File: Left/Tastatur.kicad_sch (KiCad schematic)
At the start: 66 parts, among them J101 Conn_02x05_Counter_Clockwise, J102 Conn_01x04_Pin, J103 XT60PW-M, Q101 SI2301CDS-T1-GE3, Q102 SI2301CDS-T1-GE3, Q103 SI2301CDS-T1-GE3, Q104 SI2301CDS-T1-GE3, Q105 SI2301CDS-T1-GE3, Q106 2N7002HW, Q107 SI2301CDS-T1-GE3, SW221 MK-12C02-G020, U101 USBLC6-2SC6, U102 CH592F, U103 AP2112K-3.3, U104 MT3608, U105 TP4056-42-ESOP8, U106 CD4052B, U107 LM393, Y101 32MHz

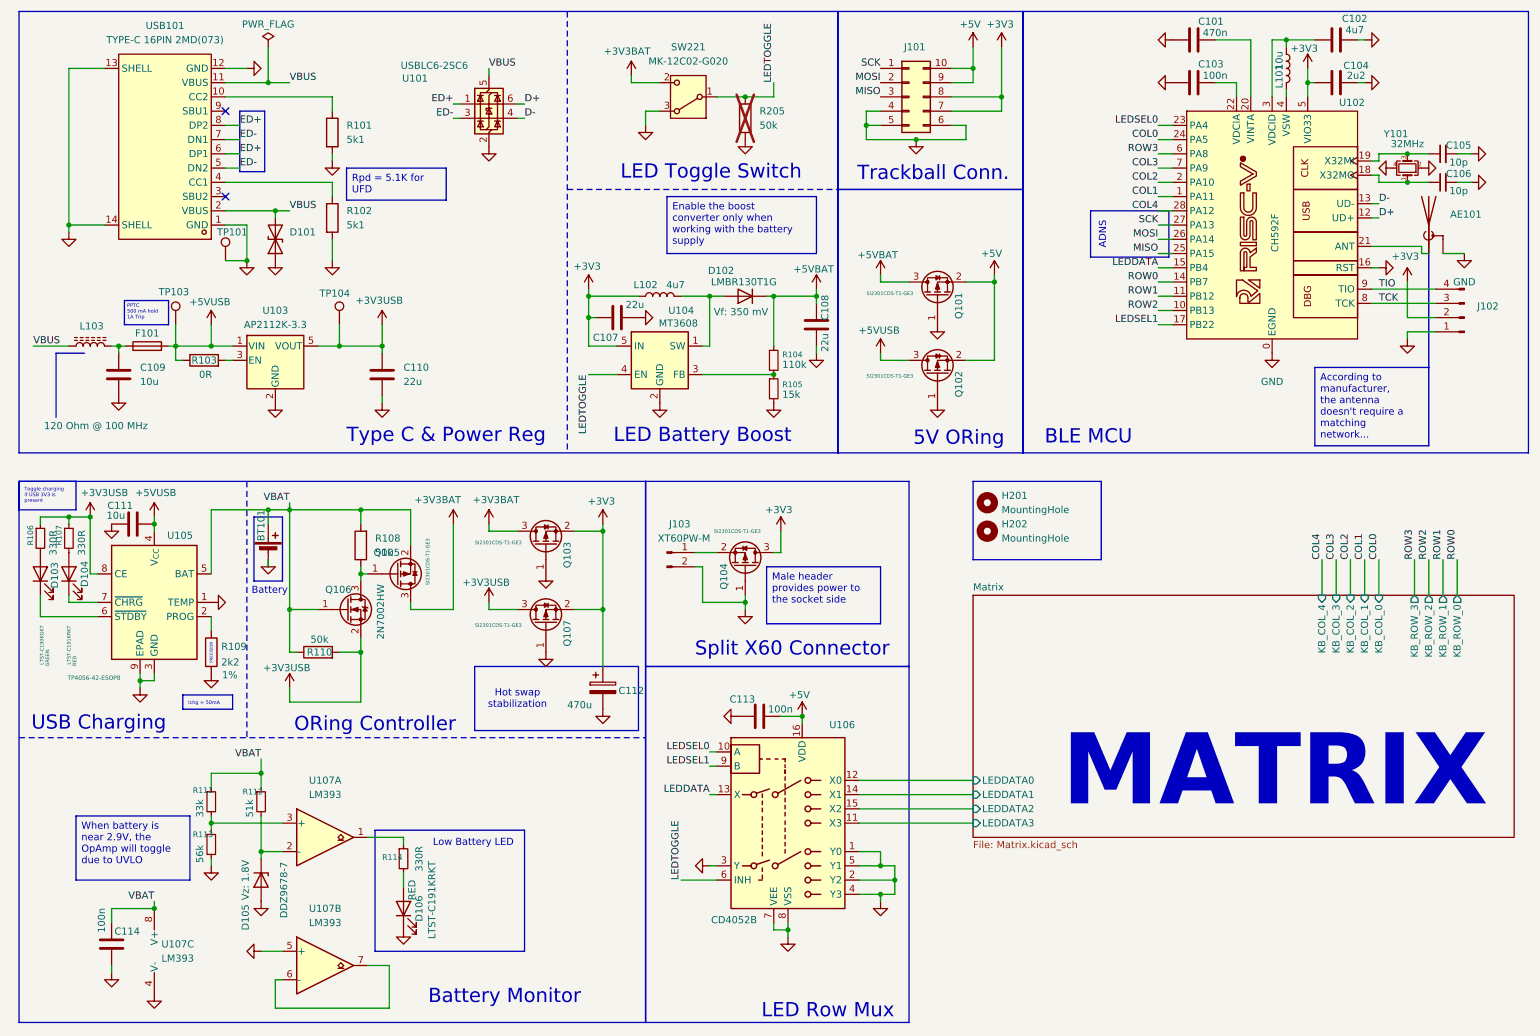
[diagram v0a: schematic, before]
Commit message: update design to use CH582F
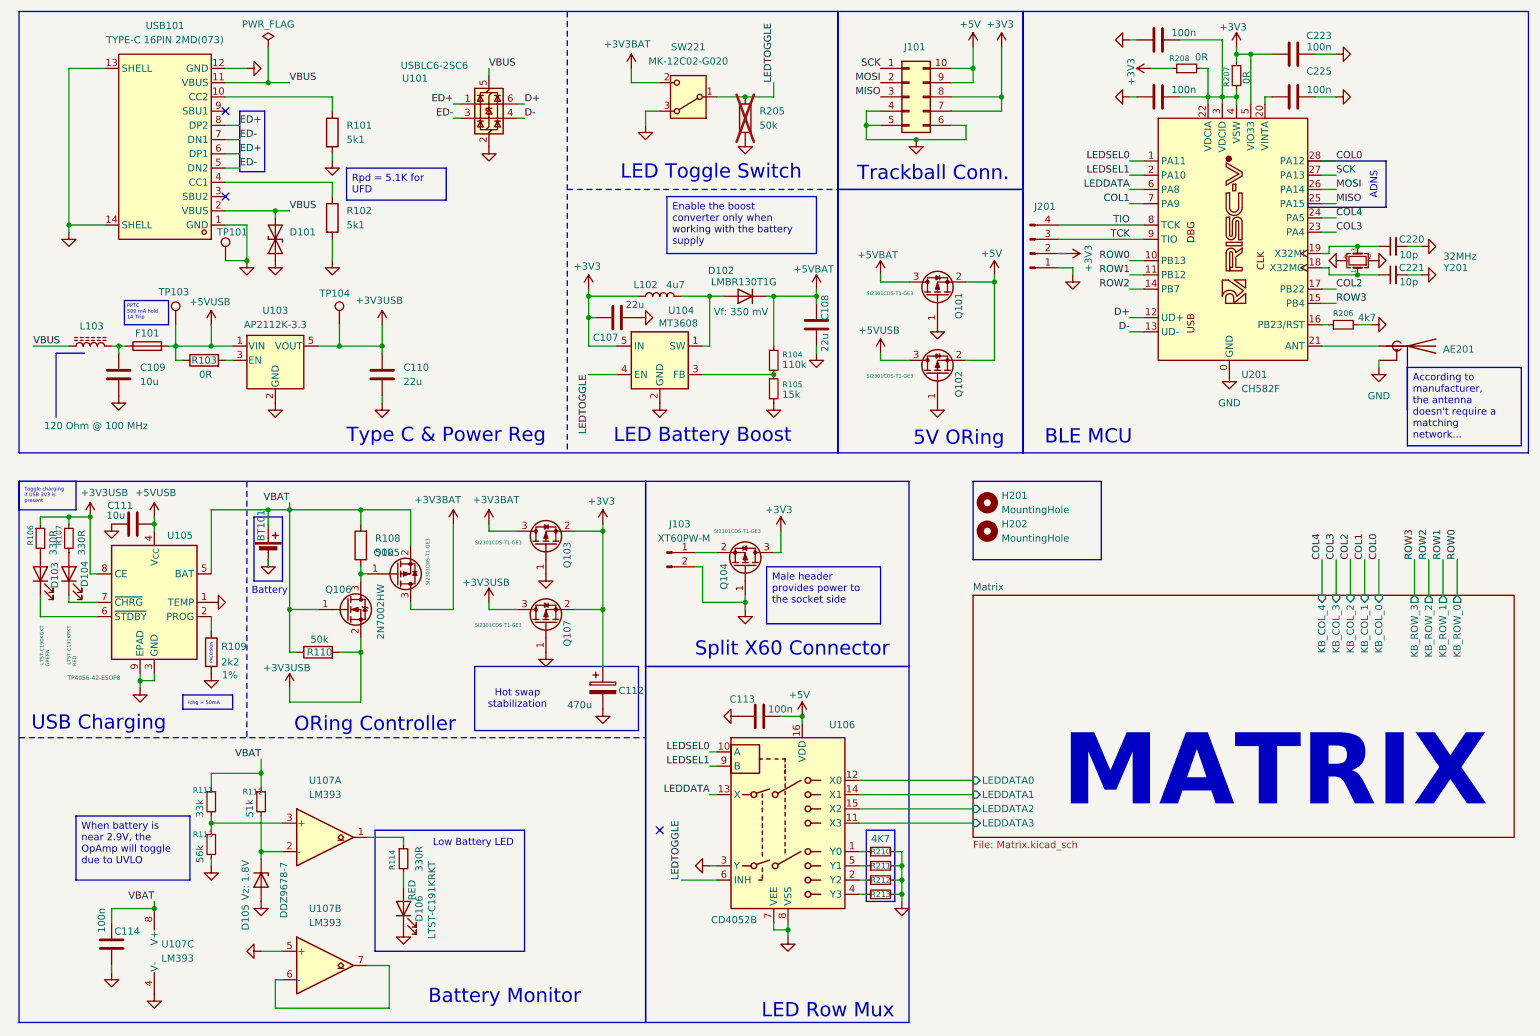
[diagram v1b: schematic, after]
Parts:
- removed AE101: Antenna_Shield, Inductor_SMD:L_1206_3216Metric, symbol Device:Antenna_Shield
- removed C101: 470n, Capacitor_SMD:C_0603_1608Metric_Pad1.08x0.95mm_HandSolder, symbol Device:C
- removed C102: 4u7, Capacitor_SMD:C_0603_1608Metric_Pad1.08x0.95mm_HandSolder, symbol Device:C
- removed C103: 100n, Capacitor_SMD:C_0603_1608Metric_Pad1.08x0.95mm_HandSolder, symbol Device:C
- removed C104: 2u2, Capacitor_SMD:C_0603_1608Metric_Pad1.08x0.95mm_HandSolder, symbol Device:C
- removed C105, C106: 10p, Capacitor_SMD:C_0603_1608Metric_Pad1.08x0.95mm_HandSolder, symbol Device:C_Small
- removed J102: Conn_01x04_Pin, Connector_JST:JST_PH_B4B-PH-K_1x04_P2.00mm_Vertical, symbol Connector:Conn_01x04_Pin
- removed L101: 10u, Inductor_SMD:L_0603_1608Metric_Pad1.05x0.95mm_HandSolder, symbol Device:L
- removed U102: CH592F, steew:CH592F, symbol steew:CH592F
- removed Y101: 32MHz, Crystal:Crystal_SMD_2016-4Pin_2.0x1.6mm, symbol Device:Crystal_GND24_Small
- added AE201: Antenna_Shield, Inductor_SMD:L_1206_3216Metric, symbol Device:Antenna_Shield
- added C220, C221: 10p, Capacitor_SMD:C_0603_1608Metric_Pad1.08x0.95mm_HandSolder, symbol Device:C_Small
- added C222, C223, C225, C226: 100n, Capacitor_SMD:C_0603_1608Metric_Pad1.08x0.95mm_HandSolder, symbol Device:C
- added J201: Conn_01x04_Pin, Connector_JST:JST_PH_B4B-PH-K_1x04_P2.00mm_Vertical, symbol Connector:Conn_01x04_Pin
- added R206: 4k7, Resistor_SMD:R_0603_1608Metric_Pad0.98x0.95mm_HandSolder, symbol Device:R_Small
- added R207, R208: 0R, Resistor_SMD:R_0603_1608Metric_Pad0.98x0.95mm_HandSolder, symbol Device:R_Small
- added R210, R211, R212, R213: 4K7, Resistor_SMD:R_0603_1608Metric_Pad0.98x0.95mm_HandSolder, symbol Device:R_Small
- added U201: CH582F, steew:CH582F, symbol steew:CH582F
- added Y201: 32MHz, Crystal:Crystal_SMD_2016-4Pin_2.0x1.6mm, symbol Device:Crystal_GND24_Small
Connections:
- net +3V3: now also C223.2, J201.2 (Pin_2), R207.1, R208.1, U201.5 (VIO33)
- net COL0: now also U201.28 (PA12)
- net COL1: now also U201.7 (PA9)
- net COL2: now also U201.17 (PB22)
- net COL3: now also U201.23 (PA4)
- net COL4: now also U201.24 (PA5)
- net D+: now also U201.12 (UD+)
- net D-: now also U201.13 (UD-)
- net GND: now also AE201.2 (Shield), C220.2, C221.2, C222.2, C223.1, C225.1, C226.2, J201.1 (Pin_1), R206.2, R210.2, R211.2, R212.2, R213.2, U201.0 (GND), Y201.2, Y201.4; no longer U106.1 (Y0), U106.2 (Y2), U106.4 (Y3), U106.5 (Y1)
- net LEDDATA: now also U201.6 (PA8)
- net LEDSEL0: now also U201.1 (PA11)
- net LEDSEL1: now also U201.2 (PA10)
- net MISO: now also U201.25 (PA15)
- net MOSI: now also U201.26 (PA14)
- net ROW0: now also U201.10 (PB13)
- net ROW1: now also U201.11 (PB12)
- net ROW2: now also U201.14 (PB7)
- net ROW3: now also U201.15 (PB4)
- net SCK: now also U201.27 (PA13)
- net TCK: now also J201.3 (Pin_3), U201.9 (TIO)
- net TIO: now also J201.4 (Pin_4), U201.8 (TCK)
- new net: R211.1, U106.5 (Y1)
- new net: R206.1, U201.16 (PB23/RST)
- new net: C222.1, C226.1, R207.2, R208.2, U201.22 (VDCIA), U201.3 (VDCID), U201.4 (VSW)
- new net: C221.1, U201.18 (X32MO), Y201.1
- new net: C220.1, U201.19 (X32MI), Y201.3
- new net: C225.2, U201.20 (VINTA)
- new net: AE201.1 (A), U201.21 (ANT)
- new net: R210.1, U106.1 (Y0)
- new net: R212.1, U106.2 (Y2)
- new net: R213.1, U106.4 (Y3)
- no-connect marks 2 -> 3

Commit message: redesign with smaller components
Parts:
- removed AE201: Antenna_Shield, Inductor_SMD:L_1206_3216Metric, symbol Device:Antenna_Shield
- removed C220, C221: 10p, Capacitor_SMD:C_0603_1608Metric_Pad1.08x0.95mm_HandSolder, symbol Device:C_Small
- removed C222, C223, C225, C226: 100n, Capacitor_SMD:C_0603_1608Metric_Pad1.08x0.95mm_HandSolder, symbol Device:C
- removed J101: Conn_02x05_Counter_Clockwise, symbol Connector_Generic:Conn_02x05_Counter_Clockwise
- removed J201: Conn_01x04_Pin, Connector_JST:JST_PH_B4B-PH-K_1x04_P2.00mm_Vertical, symbol Connector:Conn_01x04_Pin
- removed Q101, Q102, Q103, Q104, Q105, Q107: SI2301CDS-T1-GE3, Package_TO_SOT_SMD:SOT-23_Handsoldering, symbol Transistor_FET:Q_PMOS_GSD
- removed R206: 4k7, Resistor_SMD:R_0603_1608Metric_Pad0.98x0.95mm_HandSolder, symbol Device:R_Small
- removed R207, R208: 0R, Resistor_SMD:R_0603_1608Metric_Pad0.98x0.95mm_HandSolder, symbol Device:R_Small
- removed U201: CH582F, steew:CH582F, symbol steew:CH582F
- removed Y201: 32MHz, Crystal:Crystal_SMD_2016-4Pin_2.0x1.6mm, symbol Device:Crystal_GND24_Small
- added Q1, Q2, Q8: NTJD4152PT1G, Package_TO_SOT_SMD:SOT-363_SC-70-6_Handsoldering, symbol Transistor_FET:Q_Dual_PMOS_S1G1D2S2G2D1
- C10: renamed from C109; footprint Capacitor_SMD:C_0603_1608Metric_Pad1.08x0.95mm_HandSolder -> Capacitor_SMD:C_0402_1005Metric_Pad0.74x0.62mm_HandSolder
- C11: renamed from C110; footprint Capacitor_SMD:C_0603_1608Metric_Pad1.08x0.95mm_HandSolder -> Capacitor_SMD:C_0402_1005Metric_Pad0.74x0.62mm_HandSolder
- C12: renamed from C111; footprint Capacitor_SMD:C_0603_1608Metric_Pad1.08x0.95mm_HandSolder -> Capacitor_SMD:C_0402_1005Metric_Pad0.74x0.62mm_HandSolder
- C13: renamed from C112; footprint Capacitor_SMD:CP_Elec_6.3x7.7 -> Capacitor_Tantalum_SMD:CP_EIA-6032-28_Kemet-C_HandSolder
- C14: renamed from C113; footprint Capacitor_SMD:C_0603_1608Metric_Pad1.08x0.95mm_HandSolder -> Capacitor_SMD:C_0402_1005Metric_Pad0.74x0.62mm_HandSolder
- C15: renamed from C114; footprint Capacitor_SMD:C_0603_1608Metric_Pad1.08x0.95mm_HandSolder -> Capacitor_SMD:C_0402_1005Metric_Pad0.74x0.62mm_HandSolder
- C7: renamed from C107; footprint Capacitor_SMD:C_0603_1608Metric_Pad1.08x0.95mm_HandSolder -> Capacitor_SMD:C_0402_1005Metric_Pad0.74x0.62mm_HandSolder
- C8: renamed from C108; footprint Capacitor_SMD:C_0603_1608Metric_Pad1.08x0.95mm_HandSolder -> Capacitor_SMD:C_0402_1005Metric_Pad0.74x0.62mm_HandSolder
- R10: renamed from R108; footprint Resistor_SMD:R_0603_1608Metric_Pad0.98x0.95mm_HandSolder -> Resistor_SMD:R_0402_1005Metric_Pad0.72x0.64mm_HandSolder
- R11: renamed from R109; footprint Resistor_SMD:R_0603_1608Metric_Pad0.98x0.95mm_HandSolder -> Resistor_SMD:R_0402_1005Metric_Pad0.72x0.64mm_HandSolder
- R12: renamed from R110; footprint Resistor_SMD:R_0603_1608Metric_Pad0.98x0.95mm_HandSolder -> Resistor_SMD:R_0402_1005Metric_Pad0.72x0.64mm_HandSolder
- R13: renamed from R111; footprint Resistor_SMD:R_0603_1608Metric_Pad0.98x0.95mm_HandSolder -> Resistor_SMD:R_0402_1005Metric_Pad0.72x0.64mm_HandSolder
- R14: renamed from R112; footprint Resistor_SMD:R_0603_1608Metric_Pad0.98x0.95mm_HandSolder -> Resistor_SMD:R_0402_1005Metric_Pad0.72x0.64mm_HandSolder
- R15: renamed from R113; footprint Resistor_SMD:R_0603_1608Metric_Pad0.98x0.95mm_HandSolder -> Resistor_SMD:R_0402_1005Metric_Pad0.72x0.64mm_HandSolder
- R16: renamed from R210; footprint Resistor_SMD:R_0603_1608Metric_Pad0.98x0.95mm_HandSolder -> Resistor_SMD:R_0402_1005Metric_Pad0.72x0.64mm_HandSolder
- R17: renamed from R114; footprint Resistor_SMD:R_0603_1608Metric_Pad0.98x0.95mm_HandSolder -> Resistor_SMD:R_0402_1005Metric_Pad0.72x0.64mm_HandSolder
- R18: renamed from R211; footprint Resistor_SMD:R_0603_1608Metric_Pad0.98x0.95mm_HandSolder -> Resistor_SMD:R_0402_1005Metric_Pad0.72x0.64mm_HandSolder
- R19: renamed from R212; footprint Resistor_SMD:R_0603_1608Metric_Pad0.98x0.95mm_HandSolder -> Resistor_SMD:R_0402_1005Metric_Pad0.72x0.64mm_HandSolder
- R2: renamed from R205; footprint Resistor_SMD:R_0603_1608Metric_Pad0.98x0.95mm_HandSolder -> Resistor_SMD:R_0402_1005Metric_Pad0.72x0.64mm_HandSolder
- R20: renamed from R213; footprint Resistor_SMD:R_0603_1608Metric_Pad0.98x0.95mm_HandSolder -> Resistor_SMD:R_0402_1005Metric_Pad0.72x0.64mm_HandSolder
- R3: renamed from R101; footprint Resistor_SMD:R_0603_1608Metric_Pad0.98x0.95mm_HandSolder -> Resistor_SMD:R_0402_1005Metric_Pad0.72x0.64mm_HandSolder
- R4: renamed from R102; footprint Resistor_SMD:R_0603_1608Metric_Pad0.98x0.95mm_HandSolder -> Resistor_SMD:R_0402_1005Metric_Pad0.72x0.64mm_HandSolder
- R5: renamed from R103; footprint Resistor_SMD:R_0603_1608Metric_Pad0.98x0.95mm_HandSolder -> Resistor_SMD:R_0402_1005Metric_Pad0.72x0.64mm_HandSolder
- R6: renamed from R104; footprint Resistor_SMD:R_0603_1608Metric_Pad0.98x0.95mm_HandSolder -> Resistor_SMD:R_0402_1005Metric_Pad0.72x0.64mm_HandSolder
- R7: renamed from R105; footprint Resistor_SMD:R_0603_1608Metric_Pad0.98x0.95mm_HandSolder -> Resistor_SMD:R_0402_1005Metric_Pad0.72x0.64mm_HandSolder
- R8: renamed from R106; footprint Resistor_SMD:R_0603_1608Metric_Pad0.98x0.95mm_HandSolder -> Resistor_SMD:R_0402_1005Metric_Pad0.72x0.64mm_HandSolder
- R9: renamed from R107; footprint Resistor_SMD:R_0603_1608Metric_Pad0.98x0.95mm_HandSolder -> Resistor_SMD:R_0402_1005Metric_Pad0.72x0.64mm_HandSolder
- renumbered BT101 to BT1, D101 to D1, D102 to D2, D103 to D3, D104 to D4, D105 to D5, D106 to D6, F101 to F1, H201 to H1, H202 to H2, J103 to J3, L102 to L1, L103 to L2, Q106 to Q6, SW221 to SW1, TP101 to TP1, TP103 to TP2, TP104 to TP3, U101 to U1, U103 to U3, U104 to U4, U105 to U5, U106 to U6, U107 to U7, USB101 to USB1
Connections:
- net +3V3: now also SW1.2 (C), Q1.3 (D), Q1.6 (D), Q2.4 (S)
- net +3V3BAT: now also Q1.1 (S), Q2.6 (D); no longer SW1.2 (C)
- net +3V3USB: now also Q1.4 (S)
- net +5V: now also Q8.3 (D), Q8.6 (D)
- net +5VBAT: now also Q8.1 (S)
- net +5VUSB: now also Q8.4 (S)
- net GND: now also Q1.2 (G), Q1.5 (G), Q2.5 (G), Q8.2 (G), Q8.5 (G)
- net VBAT: now also Q2.1 (S)
- net at J3.1 (Pin_1): now also Q2.3 (D)
- net at Q6.3 (D), R10.1: now also Q2.2 (G)
- no-connect marks 3 -> 2
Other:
- added sheet mcu (mcu.kicad_sch)
- note added: "MCU"
- note removed: "ADNS"
- note removed: "BLE MCU"
- note removed: "Trackball Conn."
- moved on the sheet: H1, H2
